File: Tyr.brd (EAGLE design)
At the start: 152.4 x 115.6 mm, 207 parts, among them J1 TYR_TYR_DISPLAY, Q1 DTC123J, SW1 BUTTON, U1 MCP1700T, U2 CONTROLLER_PRTR5V0U2X, U3 STM32F303CC, U4 MB85RC256V, U6 TYR_TPS2552, X1 CONTROLLER_USB-C-12PUSB-C-12P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, Y1 8Mhz

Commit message: Update pads
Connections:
- net GND: now also HOLE1.P$3, HOLE2.P$3, HOLE3.P$3, HOLE4.P$3, HOLE5.P$3, HOLE6.P$3, X1.P$10, X1.P$11, X1.P$12, X1.P$7
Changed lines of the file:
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@@
 <via x="141.98203125" y="32.44453125" extent="1-16" drill="0.35"/>
 <via x="143.76796875" y="32.44453125" extent="1-16" drill="0.35"/>
-<wire x1="143.321484375" y1="8.03671875" x2="143.321484375" y2="8.0546875" width="0.1524" layer="16"/>
 <wire x1="147.6375" y1="8.0546875" x2="147.6375" y2="7.7390625" width="0.1524" layer="16"/>
 <wire x1="147.6375" y1="7.7390625" x2="148.2328125" y2="7.14375" width="0.1524" layer="16"/>
@@
 <via x="12.79921875" y="33.03984375" extent="1-16" drill="0.35"/>
 <wire x1="12.79921875" y1="33.03984375" x2="11.01328125" y2="33.03984375" width="0.3048" layer="16"/>
-<wire x1="150.75" y1="95.25" x2="150.75" y2="95.25" width="0" layer="19" extent="1-16"/>
-<wire x1="150.75" y1="57.15" x2="150.75" y2="57.15" width="0" layer="19" extent="1-16"/>
-<wire x1="24.625" y1="114.04375" x2="24.625" y2="114.04375" width="0" layer="19" extent="1-16"/>
-<wire x1="24.625" y1="110.04375" x2="24.625" y2="110.04375" width="0" layer="19" extent="1-16"/>
-<wire x1="13.475" y1="114.04375" x2="13.475" y2="114.04375" width="0" layer="19" extent="1-16"/>
-<wire x1="13.475" y1="110.04375" x2="13.475" y2="110.04375" width="0" layer="19" extent="1-16"/>
-<wire x1="113.109375" y1="1.65" x2="113.109375" y2="1.65" width="0" layer="19" extent="1-16"/>
-<wire x1="1.65" y1="95.25" x2="1.65" y2="95.25" width="0" layer="19" extent="1-16"/>
-<wire x1="1.65" y1="57.15" x2="1.65" y2="57.15" width="0" layer="19" extent="1-16"/>
-<wire x1="23.8125" y1="1.65" x2="23.8125" y2="1.65" width="0" layer="19" extent="1-16"/>
+<contactref element="HOLE1" pad="P$3"/>
+<contactref element="HOLE2" pad="P$3"/>
+<contactref element="HOLE3" pad="P$3"/>
+<contactref element="HOLE4" pad="P$3"/>
+<contactref element="HOLE5" pad="P$3"/>
+<contactref element="HOLE6" pad="P$3"/>
+<contactref element="X1" pad="P$7"/>
+<contactref element="X1" pad="P$10"/>
+<contactref element="X1" pad="P$11"/>
+<contactref element="X1" pad="P$12"/>
 </signal>
 <signal name="VCC">

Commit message: Update
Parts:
- HOLE1, HOLE2: value HOLE_MOUNT_HOLE -> HOLE_MOUNT_HOLE5MM_NOTCH; device Tyr:HOLE_M3_OVAL -> Tyr:HOLE_5MM_OVAL

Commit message: Update
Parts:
- removed D1: 1N4148, Tyr:COMPONENTS_SOD-123
- removed R3: 22, Tyr:COMPONENTS_R0603
- C7, C8: value 100n -> 1u
- R2: value 22 -> 1.5k
- moved R2 4.76 mm to (150.0, 107.2)
- moved D2 2.38 mm to (147.0, 73.8)
- moved U1 2.38 mm to (147.0, 69.7)
- moved C7 1.79 mm to (149.4, 70.8)
- moved C8 1.79 mm to (144.7, 70.8)
- moved U2 0.89 mm to (150.0, 110.1)
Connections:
- removed net N$6: R2.1, U2.3, X1.DN1, X1.DN2
- removed net N$7: R3.1, U2.2, X1.DP1, X1.DP2
- net 3.3V: no longer D1.A
- net D+: now also R2.2, U2.2, X1.DP1, X1.DP2; no longer R3.2
- net D-: now also U2.3, X1.DN1, X1.DN2; no longer R2.2
- net VCC: now also R2.1; no longer D1.C
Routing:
- net N$6: track 144.5 -> 0.00 mm, vias 2 -> 0
- net D+: track 91.8 -> 235.2 mm, vias 2 -> 5
- net N$7: track 142.7 -> 0.00 mm, vias 3 -> 0
- net D-: track 98.3 -> 239.6 mm, vias 2 -> 3
- net VCC: track 336.0 -> 329.4 mm
- net GND: track 1177.3 -> 1183.7 mm, vias 59 -> 58
- net 3.3V: track 395.3 -> 391.1 mm
- net COLUMN7: track 100.4 -> 101.7 mm

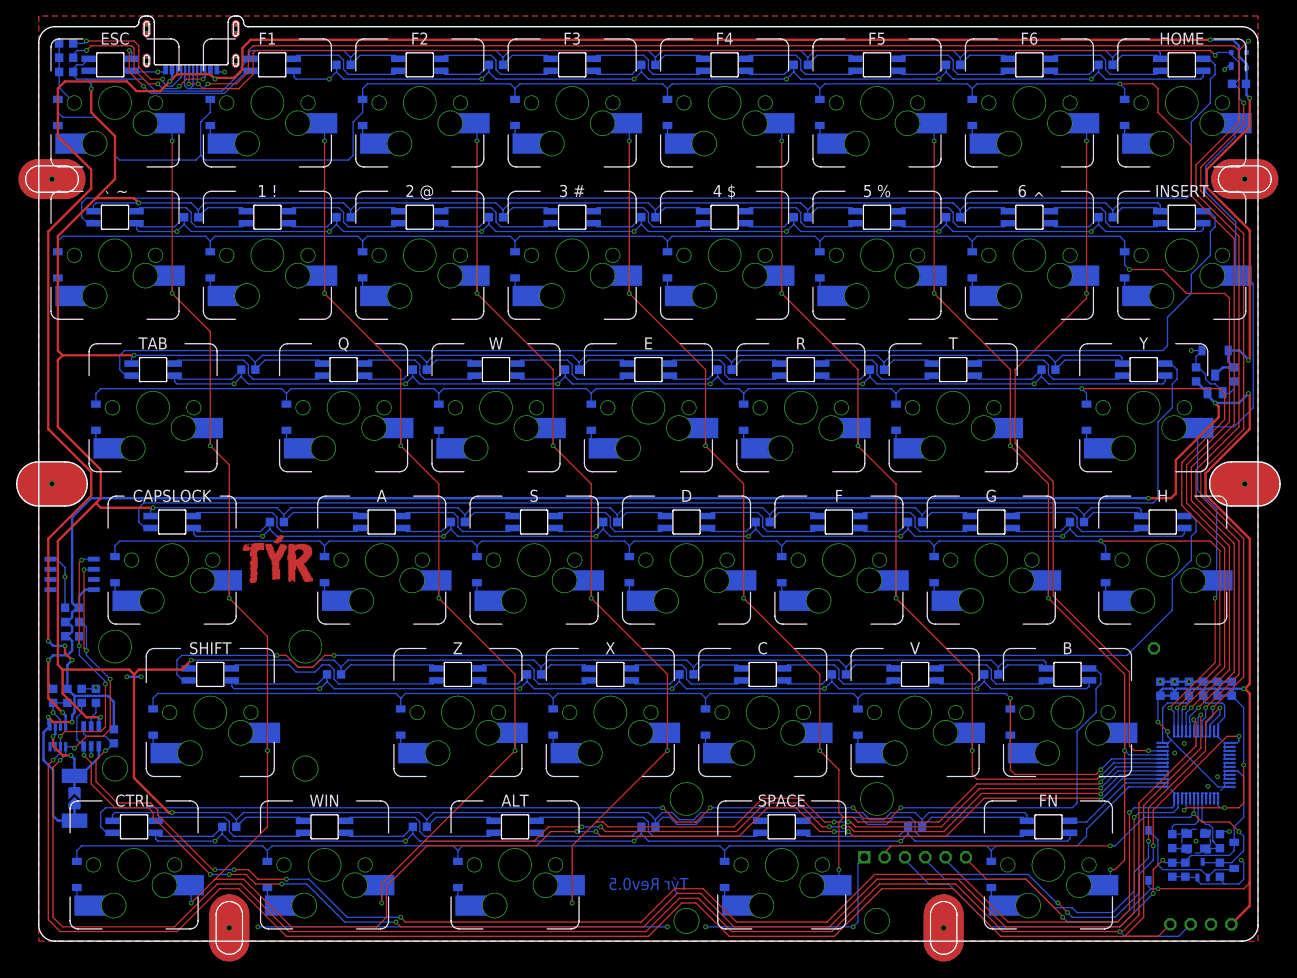
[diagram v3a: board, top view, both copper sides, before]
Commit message: USB-C shield RC filter
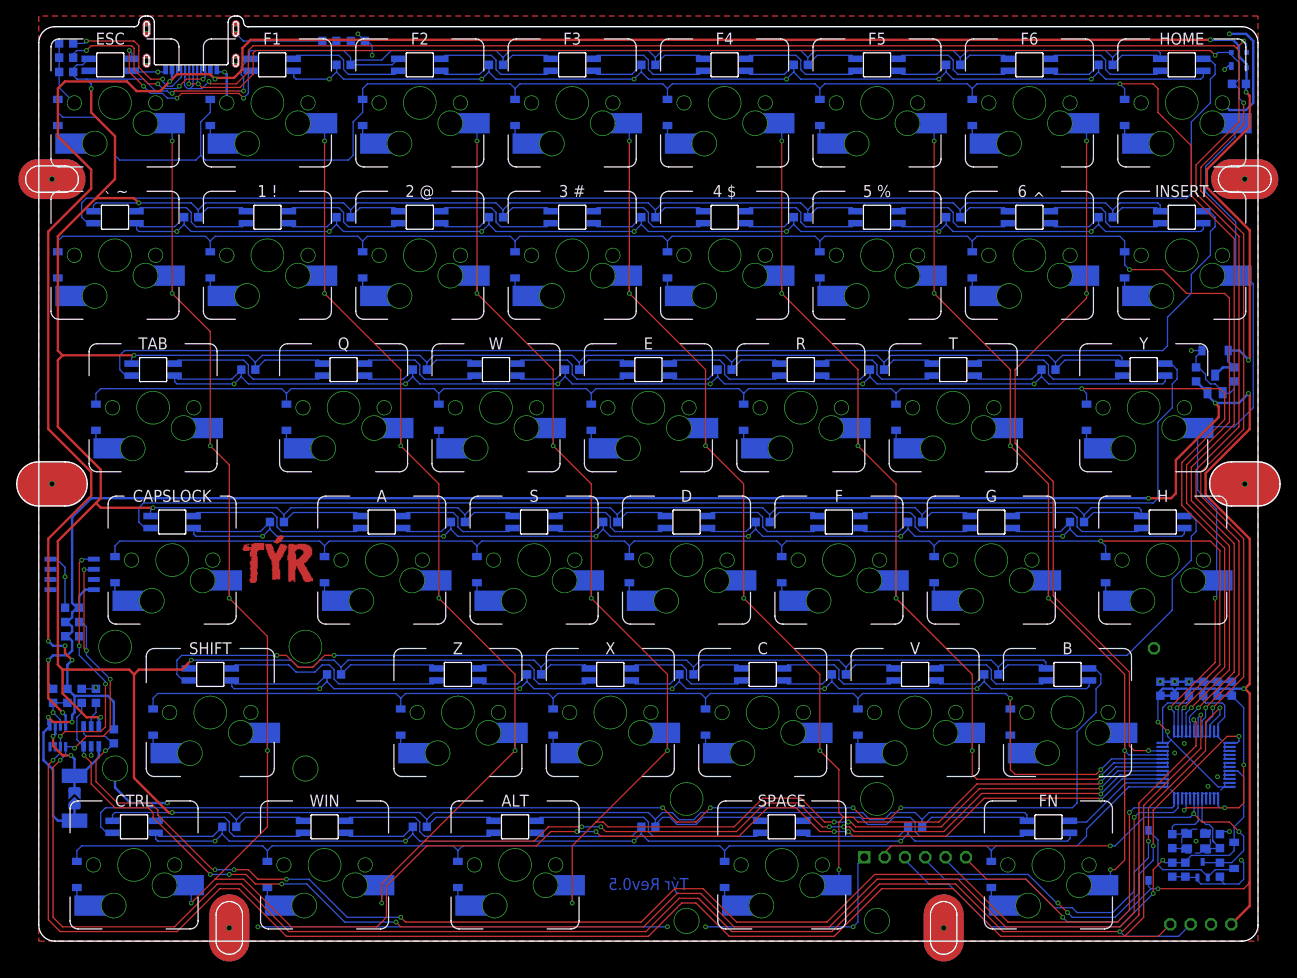
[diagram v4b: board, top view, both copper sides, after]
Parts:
- added C51: 4.7u, Tyr:COMPONENTS_C0603
- added R3: 1M, Tyr:COMPONENTS_R0603
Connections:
- new net N$6: R3.1, X1.P$12, X1.P$6, X1.P$9
- new net N$7: C51.1, R3.2
- net GND: now also C51.2; no longer HOLE1.P$1, HOLE1.P$2, HOLE1.P$3, HOLE2.P$1, HOLE2.P$2, HOLE2.P$3, HOLE3.P$1, HOLE3.P$2, HOLE3.P$3, HOLE4.P$1, HOLE4.P$2, HOLE4.P$3, HOLE5.P$1, HOLE5.P$2, HOLE5.P$3, HOLE6.P$1, HOLE6.P$2, HOLE6.P$3, X1.P$1, X1.P$10, X1.P$11, X1.P$12, X1.P$2, X1.P$3, X1.P$4, X1.P$5, X1.P$6, X1.P$7, X1.P$8, X1.P$9
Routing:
- net GND: track 1183.7 -> 1214.7 mm, vias 58 -> 60
- net N$6: track 0.00 -> 11.8 mm
- net N$88: track 21.3 -> 23.9 mm, vias 2 -> 4
- net LED_VCC: track 1227.0 -> 1229.1 mm, vias 7 -> 9
- net N$7: track 0.00 -> 1.82 mm

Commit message: Update
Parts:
- moved C51 0.30 mm to (39.9, 112.8)
- moved R3 0.30 mm to (36.3, 112.8)
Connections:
- removed net N$7: C51.1, R3.2
- net GND: now also R3.2
- net N$6: now also C51.1
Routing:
- net N$6: track 11.8 -> 16.3 mm
- net GND: track 1214.7 -> 1218.6 mm, vias 60 -> 59
- net N$88: track 23.9 -> 26.6 mm
- net N$7: track 1.82 -> 0.00 mm
- net VCC: track 329.4 -> 328.8 mm

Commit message: Update
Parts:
- added C52: 4.7u, Tyr:COMPONENTS_C0603
- added D1: 1N4148, Tyr:COMPONENTS_SOD-123
- added R5: 1M, Tyr:COMPONENTS_R0603
- moved C51 0.30 mm to (39.9, 112.5)
- moved R3 0.30 mm to (36.3, 112.5)
- renumbered PH1 to ISP_HEADER
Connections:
- net N$6 renamed SHIELD
- new net CASE: D1.A, HOLE1.P$1, HOLE1.P$2, HOLE1.P$3, HOLE2.P$1, HOLE2.P$2, HOLE2.P$3, HOLE3.P$1, HOLE3.P$2, HOLE3.P$3, HOLE4.P$1, HOLE4.P$2, HOLE4.P$3, HOLE5.P$1, HOLE5.P$2, HOLE5.P$3, HOLE6.P$1, HOLE6.P$2, HOLE6.P$3
- new net N$6: C52.1, D1.C, R5.1
- net GND: now also C52.2, R5.2
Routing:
- net CASE: track 0.00 -> 44.7 mm
- net GND: track 1218.6 -> 1211.0 mm
- net N$6: track 0.00 -> 3.89 mm
- net COLUMN7: track 101.7 -> 100.0 mm, vias 2 -> 4
- net SHIELD: track 16.3 -> 15.8 mm
- net VCC: track 328.8 -> 328.7 mm, vias 10 -> 11
- added copper zone on layer 1, net CASE
- added copper zone on layer 16, net CASE

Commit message: Update Tyr.brd
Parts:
- moved C10 0.30 mm to (4.46, 41.7)
- moved R10 0.30 mm to (4.46, 38.1)
- moved R9 0.30 mm to (4.46, 39.9)
- moved U4 0.30 mm to (4.46, 45.8)
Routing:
- net 3.3V: track 391.1 -> 392.0 mm
- net SDA: track 242.8 -> 243.6 mm

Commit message: Update
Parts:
- removed R13: 10k, Tyr:COMPONENTS_R0603
- added R6: 100k, Tyr:COMPONENTS_R0603
- C10: value 10u -> 22p
- C12: value 22p -> 4.7u
- C16: value 104 -> 4.7u
- C17: value 104 -> 10u
- C51, C52: value 4.7u -> 104
- D1: value 1N4148 -> DIODE_SCHOTTKY
- D2: value DIODE_SCHOTTKY -> 1N4148
- R10: value 10k -> 0.1/1% (PT2512FK-070R1L); device Tyr:COMPONENTS_R0603 -> Tyr:MICROBUILDER_2512
- R11: value 0.1/1% (PT2512FK-070R1L) -> 54.9k; device Tyr:MICROBUILDER_2512 -> Tyr:COMPONENTS_R0603
- R12: value 54.9k -> 10k
- R3: value 1M -> 5.1k
- R4: value 5.1k -> 1M
- R5: value 1M -> 100k
- R7, R8: value 100k -> 10k
- R9: value 10k -> 1M
- moved D3 158.9 mm to (3.57, 73.8), turned to 180 degrees
- moved R5 151.8 mm to (141.7, 8.93), turned to 270 degrees
- moved C10 146.1 mm to (147.6, 12.5), turned to 270 degrees
- moved D1 143.5 mm to (147.0, 73.8)
- moved C12 142.7 mm to (39.9, 112.5), turned to 180 degrees
- moved R7 140.7 mm to (4.46, 39.9), turned to 0 degrees
- moved C52 119.8 mm to (109.5, 14.3), turned to 180 degrees
- moved C51 104.7 mm to (76.2, 14.3)
- moved C23 97.1 mm to (114.3, 109.5)
- moved C24 97.1 mm to (133.3, 109.5)
- moved C30 90.1 mm to (114.3, 90.5)
- moved C31 87.8 mm to (133.3, 90.5)
- moved C47 78.5 mm to (100.0, 33.3)
- moved C36 77.4 mm to (104.8, 71.4)
- moved C37 76.2 mm to (126.2, 71.4)
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- renumbered ISP_HEADER to PH1, KEYSWITCH1 to SW2, KEYSWITCH10 to SW11, KEYSWITCH11 to SW12, KEYSWITCH12 to SW13, KEYSWITCH13 to SW14, KEYSWITCH14 to SW15, KEYSWITCH15 to SW16, KEYSWITCH16 to SW17, KEYSWITCH17 to SW18, KEYSWITCH18 to SW19, KEYSWITCH19 to SW20, KEYSWITCH2 to SW3, KEYSWITCH20 to SW21, KEYSWITCH21 to SW22, KEYSWITCH22 to SW23, KEYSWITCH23 to SW24, KEYSWITCH24 to SW25, KEYSWITCH25 to SW26, KEYSWITCH26 to SW27, KEYSWITCH27 to SW28, KEYSWITCH28 to SW29, KEYSWITCH29 to SW30, KEYSWITCH3 to SW4, KEYSWITCH30 to SW31, KEYSWITCH31 to SW33, KEYSWITCH32 to SW34, KEYSWITCH33 to SW35, KEYSWITCH34 to SW36, KEYSWITCH35 to SW37, KEYSWITCH36 to SW38, KEYSWITCH37 to SW39, KEYSWITCH38 to SW40, KEYSWITCH39 to SW42, KEYSWITCH4 to SW5, KEYSWITCH5 to SW6, KEYSWITCH6 to SW7, KEYSWITCH7 to SW8, KEYSWITCH8 to SW9, KEYSWITCH9 to SW10, SWITCH1 to SW32, SWITCH2 to SW41, U$1 to LOGO1
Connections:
- net 3.3V: now also C17.2, R7.2, R8.2; no longer C10.2, R10.2, R9.2
- net BOOT0: now also D2.C, R5.1; no longer D3.C, R7.1
- net CASE: now also D3.A; no longer D1.A
- net GND: now also C12.2, C16.2, C51.1, C52.1, D1.A, R11.1, R9.2; no longer C12.1, C16.1, C51.2, C52.2, D2.A, R13.1, R7.2
- net LED_ENABLE: now also R12.2; no longer R13.2
- net LED_FAULT: now also R6.1; no longer R8.1
- net LED_VCC: now also C51.2, C52.2; no longer C16.2, C17.2
- net N$2: now also R10.2; no longer R11.2
- net N$3: now also R11.2; no longer R12.2
- net N$5: now also D2.A; no longer D3.A
- net N$6: now also C16.1, D3.C, R9.1; no longer C52.1, D1.C, R5.1
- net N$89: now also R3.1; no longer R4.1
- net SCL: now also R7.1; no longer R9.1
- net SDA: now also R8.1; no longer R10.1
- net SHIELD: now also C12.1, R4.1; no longer C51.1, R3.1
- net VCC: now also D1.C, R10.1, R6.2; no longer D2.C, R11.1, R8.2
- net XTAL1: now also C10.2; no longer C11.2
- net XTAL2: now also C11.2; no longer C12.2
